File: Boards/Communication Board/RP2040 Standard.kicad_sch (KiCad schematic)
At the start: 38 parts, among them J1 BM03B-SRSS-TBLFSN, J4 DX07S016JA1R1500, U1 W25Q128JVSIQ TR, U5 ESD7L5.0DT5G, U6 ST1L05APU33R

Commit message: COMS
Acho que já está tudo de footprints que tinha que fazer na Communication Board
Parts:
- CV1, CV10, CV11, CV12, CV13, CV14, CV17, CV18, CV2, CV3, CV4, CV5, CV6, CV7, CV8, CV9: footprint Capacitor_SMD:C_0201_0603Metric -> CAP_GCM155_MUR:CAP_GCM155_MUR
- CV15, CV16: footprint Capacitor_SMD:C_0201_0603Metric -> GRM15x:GRM15x
- J1: footprint CONN_BM03B-SRSS-TBLFSN_JST -> SWD_Con:CONN_BM03B-SRSS-TBLFSN_JST
- J4: footprint DX07S016JA1R1500:JAE_DX07S016JA1R1500 -> USBC-DX07S016JA1:JAE_DX07S016JA1R1500
- R1, R4, R5, R6, R7, R8, R9, RC1: footprint Resistor_SMD:R_0201_0603Metric -> RC0402N_VIS:RC0402N_VIS
- R2, R3: footprint Resistor_SMD:R_0201_0603Metric -> KTR03EZPF27R0:RES_R0603_ROM
- S3, S4: footprint TL3305CF160QG:SW_TL3305CF160QG -> E-Switch_7mm:SW_TL3305CF160QG
- U1: footprint SOIC_208MIL_WIN -> NOR Flash:SOIC_208MIL_WIN
- U5: footprint SOT-723_0P85X1P25_ONS -> ESD7L5-Diode:SOT-723_0P85X1P25_ONS
- U6: footprint DFN_5APU33R_STM -> LDO ST1L05A:DFN_5APU33R_STM
- XTAL1: footprint ASE-3.2X2.5_ABR -> AS12MHz:ASE-3.2X2.5_ABR
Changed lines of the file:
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@@
 			)
 		)
-		(property "Footprint" "SOIC_208MIL_WIN"
+		(property "Footprint" "NOR Flash:SOIC_208MIL_WIN"
 			(at 180.975 45.72 0)
 			(effects
@@
 			)
 		)
-		(property "Footprint" "Capacitor_SMD:C_0201_0603Metric"
+		(property "Footprint" "CAP_GCM155_MUR:CAP_GCM155_MUR"
 			(at 132.08 177.4698 0)
 			(effects
@@
 			)
 		)
-		(property "Footprint" "DX07S016JA1R1500:JAE_DX07S016JA1R1500"
+		(property "Footprint" "USBC-DX07S016JA1:JAE_DX07S016JA1R1500"
 			(at 235.585 134.62 0)
 			(effects
@@
 			)
 		)
-		(property "Footprint" "Capacitor_SMD:C_0201_0603Metric"
+		(property "Footprint" "CAP_GCM155_MUR:CAP_GCM155_MUR"
 			(at 94.3102 50.165 0)
 			(effects
@@
 			)
 		)
-		(property "Footprint" "Capacitor_SMD:C_0201_0603Metric"
+		(property "Footprint" "CAP_GCM155_MUR:CAP_GCM155_MUR"
 			(at 32.6898 61.595 0)
 			(effects
@@
 			)
 		)
-		(property "Footprint" "ASE-3.2X2.5_ABR"
+		(property "Footprint" "AS12MHz:ASE-3.2X2.5_ABR"
 			(at 57.15 182.88 0)
 			(effects
@@
 			)
 		)
-		(property "Footprint" "Resistor_SMD:R_0201_0603Metric"
+		(property "Footprint" "KTR03EZPF27R0:RES_R0603_ROM"
 			(at 41.275 78.867 90)
 			(effects
@@
 			)
 		)
-		(property "Footprint" "Capacitor_SMD:C_0201_0603Metric"
+		(property "Footprint" "CAP_GCM155_MUR:CAP_GCM155_MUR"
 			(at 64.4398 42.545 0)
 			(effects
@@
 			)
 		)
-		(property "Footprint" "Capacitor_SMD:C_0201_0603Metric"
+		(property "Footprint" "CAP_GCM155_MUR:CAP_GCM155_MUR"
 			(at 101.2952 50.165 0)
 			(effects
@@
 			)
 		)
-		(property "Footprint" "SOT-723_0P85X1P25_ONS"
+		(property "Footprint" "ESD7L5-Diode:SOT-723_0P85X1P25_ONS"
 			(at 202.565 136.525 0)
 			(effects
@@
 			)
 		)
-		(property "Footprint" "Capacitor_SMD:C_0201_0603Metric"
+		(property "Footprint" "CAP_GCM155_MUR:CAP_GCM155_MUR"
 			(at 122.2502 50.165 0)
 			(effects
@@
 			)
 		)
-		(property "Footprint" "Capacitor_SMD:C_0201_0603Metric"
+		(property "Footprint" "CAP_GCM155_MUR:CAP_GCM155_MUR"
 			(at 129.2352 50.165 0)
 			(effects
@@
 			)
 		)
-		(property "Footprint" "Capacitor_SMD:C_0201_0603Metric"
+		(property "Footprint" "CAP_GCM155_MUR:CAP_GCM155_MUR"
 			(at 272.7452 41.91 0)
 			(effects
@@
 			)
 		)
-		(property "Footprint" "TL3305CF160QG:SW_TL3305CF160QG"
+		(property "Footprint" "E-Switch_7mm:SW_TL3305CF160QG"
 			(at 33.02 50.8 0)
 			(effects
@@
 			)
 		)
-		(property "Footprint" "Resistor_SMD:R_0201_0603Metric"
+		(property "Footprint" "RC0402N_VIS:RC0402N_VIS"
 			(at 55.372 177.8 90)
 			(effects
@@
 			)
 		)
-		(property "Footprint" "DFN_5APU33R_STM"
+		(property "Footprint" "LDO ST1L05A:DFN_5APU33R_STM"
 			(at 202.565 83.82 0)
 			(effects
@@
 			)
 		)
-		(property "Footprint" "Capacitor_SMD:C_0201_0603Metric"
+		(property "Footprint" "CAP_GCM155_MUR:CAP_GCM155_MUR"
 			(at 64.4652 62.23 0)
 			(effects
@@
 			)
 		)
-		(property "Footprint" "Resistor_SMD:R_0201_0603Metric"
+		(property "Footprint" "RC0402N_VIS:RC0402N_VIS"
 			(at 183.642 135.89 90)
 			(effects
@@
 			)
 		)
-		(property "Footprint" "Capacitor_SMD:C_0201_0603Metric"
+		(property "Footprint" "CAP_GCM155_MUR:CAP_GCM155_MUR"
 			(at 136.2202 50.165 0)
 			(effects
@@
 			)
 		)
-		(property "Footprint" "Capacitor_SMD:C_0201_0603Metric"
+		(property "Footprint" "CAP_GCM155_MUR:CAP_GCM155_MUR"
 			(at 87.3252 50.165 0)
 			(effects
@@
 			)
 		)
-		(property "Footprint" "Resistor_SMD:R_0201_0603Metric"
+		(property "Footprint" "KTR03EZPF27R0:RES_R0603_ROM"
 			(at 41.275 79.883 90)
 			(effects
@@
 			)
 		)
-		(property "Footprint" "Capacitor_SMD:C_0201_0603Metric"
+		(property "Footprint" "CAP_GCM155_MUR:CAP_GCM155_MUR"
 			(at 190.1698 89.535 0)
 			(effects
@@
 			)
 		)
-		(property "Footprint" "TL3305CF160QG:SW_TL3305CF160QG"
+		(property "Footprint" "E-Switch_7mm:SW_TL3305CF160QG"
 			(at 161.925 31.75 0)
 			(effects
@@
 			)
 		)
-		(property "Footprint" "CONN_BM03B-SRSS-TBLFSN_JST"
+		(property "Footprint" "SWD_Con:CONN_BM03B-SRSS-TBLFSN_JST"
 			(at 35.56 140.335 0)
 			(effects
@@
 			)
 		)
-		(property "Footprint" "Capacitor_SMD:C_0201_0603Metric"
+		(property "Footprint" "GRM15x:GRM15x"
 			(at 177.4698 90.17 0)
 			(effects
@@
 			)
 		)
-		(property "Footprint" "Resistor_SMD:R_0201_0603Metric"
+		(property "Footprint" "RC0402N_VIS:RC0402N_VIS"
 			(at 41.91 133.477 90)
 			(effects
@@
 			)
 		)
-		(property "Footprint" "Capacitor_SMD:C_0201_0603Metric"
+		(property "Footprint" "CAP_GCM155_MUR:CAP_GCM155_MUR"
 			(at 56.8198 42.545 0)
 			(effects
@@
 			)
 		)
-		(property "Footprint" "Resistor_SMD:R_0201_0603Metric"
+		(property "Footprint" "RC0402N_VIS:RC0402N_VIS"
 			(at 43.942 64.77 90)
 			(effects
@@
 			)
 		)
-		(property "Footprint" "Resistor_SMD:R_0201_0603Metric"
+		(property "Footprint" "RC0402N_VIS:RC0402N_VIS"
 			(at 177.927 40.005 90)
 			(effects
@@
 			)
 		)
-		(property "Footprint" "Capacitor_SMD:C_0201_0603Metric"
+		(property "Footprint" "CAP_GCM155_MUR:CAP_GCM155_MUR"
 			(at 115.2652 50.165 0)
 			(effects
@@
 			)
 		)
-		(property "Footprint" "Capacitor_SMD:C_0201_0603Metric"
+		(property "Footprint" "GRM15x:GRM15x"
 			(at 190.1698 85.725 0)
 			(effects
@@
 			)
 		)
-		(property "Footprint" "Resistor_SMD:R_0201_0603Metric"
+		(property "Footprint" "RC0402N_VIS:RC0402N_VIS"
 			(at 189.357 137.795 90)
 			(effects
@@
 			)
 		)
-		(property "Footprint" "Capacitor_SMD:C_0201_0603Metric"
+		(property "Footprint" "CAP_GCM155_MUR:CAP_GCM155_MUR"
 			(at 108.2802 50.165 0)
 			(effects
@@
 			)
 		)
-		(property "Footprint" "Resistor_SMD:R_0201_0603Metric"
+		(property "Footprint" "RC0402N_VIS:RC0402N_VIS"
 			(at 18.542 65.405 90)
 			(effects
@@
 			)
 		)
-		(property "Footprint" "Capacitor_SMD:C_0201_0603Metric"
+		(property "Footprint" "CAP_GCM155_MUR:CAP_GCM155_MUR"
 			(at 87.3252 59.69 0)
 			(effects
@@
 			)
 		)
-		(property "Footprint" "Resistor_SMD:R_0201_0603Metric"
+		(property "Footprint" "RC0402N_VIS:RC0402N_VIS"
 			(at 41.91 138.557 90)
 			(effects

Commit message: Mudança de nome das footprints
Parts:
- CV1, CV10, CV11, CV12, CV13, CV14, CV17, CV18, CV2, CV3, CV4, CV5, CV6, CV7, CV8, CV9: footprint CAP_GCM155_MUR:CAP_GCM155_MUR -> Capacitor_0402:Capacitor_0402
- CV15, CV16: footprint GRM15x:GRM15x -> C_4uF7_0402:C_4uF7_0402
- R1, R4, R5, R6, R7, R8: footprint RC0402N_VIS:RC0402N_VIS -> RES_0402:RES_0402
- R2, R3: footprint KTR03EZPF27R0:RES_R0603_ROM -> RES_R0603_27:RES_R0603_27
- R9, RC1: footprint RC0402N_VIS:RC0402N_VIS -> R_0805_5K1:R_0805_5K1
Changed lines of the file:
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@@
 			)
 		)
-		(property "Footprint" "CAP_GCM155_MUR:CAP_GCM155_MUR"
+		(property "Footprint" "Capacitor_0402:Capacitor_0402"
 			(at 132.08 177.4698 0)
 			(effects
@@
 			)
 		)
-		(property "Footprint" "CAP_GCM155_MUR:CAP_GCM155_MUR"
+		(property "Footprint" "Capacitor_0402:Capacitor_0402"
 			(at 94.3102 50.165 0)
 			(effects
@@
 			)
 		)
-		(property "Footprint" "CAP_GCM155_MUR:CAP_GCM155_MUR"
+		(property "Footprint" "Capacitor_0402:Capacitor_0402"
 			(at 32.6898 61.595 0)
 			(effects
@@
 			)
 		)
-		(property "Footprint" "KTR03EZPF27R0:RES_R0603_ROM"
+		(property "Footprint" "RES_R0603_27:RES_R0603_27"
 			(at 41.275 78.867 90)
 			(effects
@@
 			)
 		)
-		(property "Footprint" "CAP_GCM155_MUR:CAP_GCM155_MUR"
+		(property "Footprint" "Capacitor_0402:Capacitor_0402"
 			(at 64.4398 42.545 0)
 			(effects
@@
 			)
 		)
-		(property "Footprint" "CAP_GCM155_MUR:CAP_GCM155_MUR"
+		(property "Footprint" "Capacitor_0402:Capacitor_0402"
 			(at 101.2952 50.165 0)
 			(effects
@@
 			)
 		)
-		(property "Footprint" "CAP_GCM155_MUR:CAP_GCM155_MUR"
+		(property "Footprint" "Capacitor_0402:Capacitor_0402"
 			(at 122.2502 50.165 0)
 			(effects
@@
 			)
 		)
-		(property "Footprint" "CAP_GCM155_MUR:CAP_GCM155_MUR"
+		(property "Footprint" "Capacitor_0402:Capacitor_0402"
 			(at 129.2352 50.165 0)
 			(effects
@@
 			)
 		)
-		(property "Footprint" "CAP_GCM155_MUR:CAP_GCM155_MUR"
+		(property "Footprint" "Capacitor_0402:Capacitor_0402"
 			(at 272.7452 41.91 0)
 			(effects
@@
 			)
 		)
-		(property "Footprint" "RC0402N_VIS:RC0402N_VIS"
+		(property "Footprint" "RES_0402:RES_0402"
 			(at 55.372 177.8 90)
 			(effects
@@
 			)
 		)
-		(property "Footprint" "CAP_GCM155_MUR:CAP_GCM155_MUR"
+		(property "Footprint" "Capacitor_0402:Capacitor_0402"
 			(at 64.4652 62.23 0)
 			(effects
@@
 			)
 		)
-		(property "Footprint" "RC0402N_VIS:RC0402N_VIS"
+		(property "Footprint" "R_0805_5K1:R_0805_5K1"
 			(at 183.642 135.89 90)
 			(effects
@@
 			)
 		)
-		(property "Footprint" "CAP_GCM155_MUR:CAP_GCM155_MUR"
+		(property "Footprint" "Capacitor_0402:Capacitor_0402"
 			(at 136.2202 50.165 0)
 			(effects
@@
 			)
 		)
-		(property "Footprint" "CAP_GCM155_MUR:CAP_GCM155_MUR"
+		(property "Footprint" "Capacitor_0402:Capacitor_0402"
 			(at 87.3252 50.165 0)
 			(effects
@@
 			)
 		)
-		(property "Footprint" "KTR03EZPF27R0:RES_R0603_ROM"
+		(property "Footprint" "RES_R0603_27:RES_R0603_27"
 			(at 41.275 79.883 90)
 			(effects
@@
 			)
 		)
-		(property "Footprint" "CAP_GCM155_MUR:CAP_GCM155_MUR"
+		(property "Footprint" "Capacitor_0402:Capacitor_0402"
 			(at 190.1698 89.535 0)
 			(effects
@@
 			)
 		)
-		(property "Footprint" "GRM15x:GRM15x"
+		(property "Footprint" "C_4uF7_0402:C_4uF7_0402"
 			(at 177.4698 90.17 0)
 			(effects
@@
 			)
 		)
-		(property "Footprint" "RC0402N_VIS:RC0402N_VIS"
+		(property "Footprint" "RES_0402:RES_0402"
 			(at 41.91 133.477 90)
 			(effects
@@
 			)
 		)
-		(property "Footprint" "CAP_GCM155_MUR:CAP_GCM155_MUR"
+		(property "Footprint" "Capacitor_0402:Capacitor_0402"
 			(at 56.8198 42.545 0)
 			(effects
@@
 			)
 		)
-		(property "Footprint" "RC0402N_VIS:RC0402N_VIS"
+		(property "Footprint" "RES_0402:RES_0402"
 			(at 43.942 64.77 90)
 			(effects
@@
 			)
 		)
-		(property "Footprint" "RC0402N_VIS:RC0402N_VIS"
+		(property "Footprint" "RES_0402:RES_0402"
 			(at 177.927 40.005 90)
 			(effects
@@
 			)
 		)
-		(property "Footprint" "CAP_GCM155_MUR:CAP_GCM155_MUR"
+		(property "Footprint" "Capacitor_0402:Capacitor_0402"
 			(at 115.2652 50.165 0)
 			(effects
@@
 			)
 		)
-		(property "Footprint" "GRM15x:GRM15x"
+		(property "Footprint" "C_4uF7_0402:C_4uF7_0402"
 			(at 190.1698 85.725 0)
 			(effects
@@
 			)
 		)
-		(property "Footprint" "RC0402N_VIS:RC0402N_VIS"
+		(property "Footprint" "R_0805_5K1:R_0805_5K1"
 			(at 189.357 137.795 90)
 			(effects
@@
 			)
 		)
-		(property "Footprint" "CAP_GCM155_MUR:CAP_GCM155_MUR"
+		(property "Footprint" "Capacitor_0402:Capacitor_0402"
 			(at 108.2802 50.165 0)
 			(effects
@@
 			)
 		)
-		(property "Footprint" "RC0402N_VIS:RC0402N_VIS"
+		(property "Footprint" "RES_0402:RES_0402"
 			(at 18.542 65.405 90)
 			(effects
@@
 			)
 		)
-		(property "Footprint" "CAP_GCM155_MUR:CAP_GCM155_MUR"
+		(property "Footprint" "Capacitor_0402:Capacitor_0402"
 			(at 87.3252 59.69 0)
 			(effects
@@
 			)
 		)
-		(property "Footprint" "RC0402N_VIS:RC0402N_VIS"
+		(property "Footprint" "RES_0402:RES_0402"
 			(at 41.91 138.557 90)
 			(effects

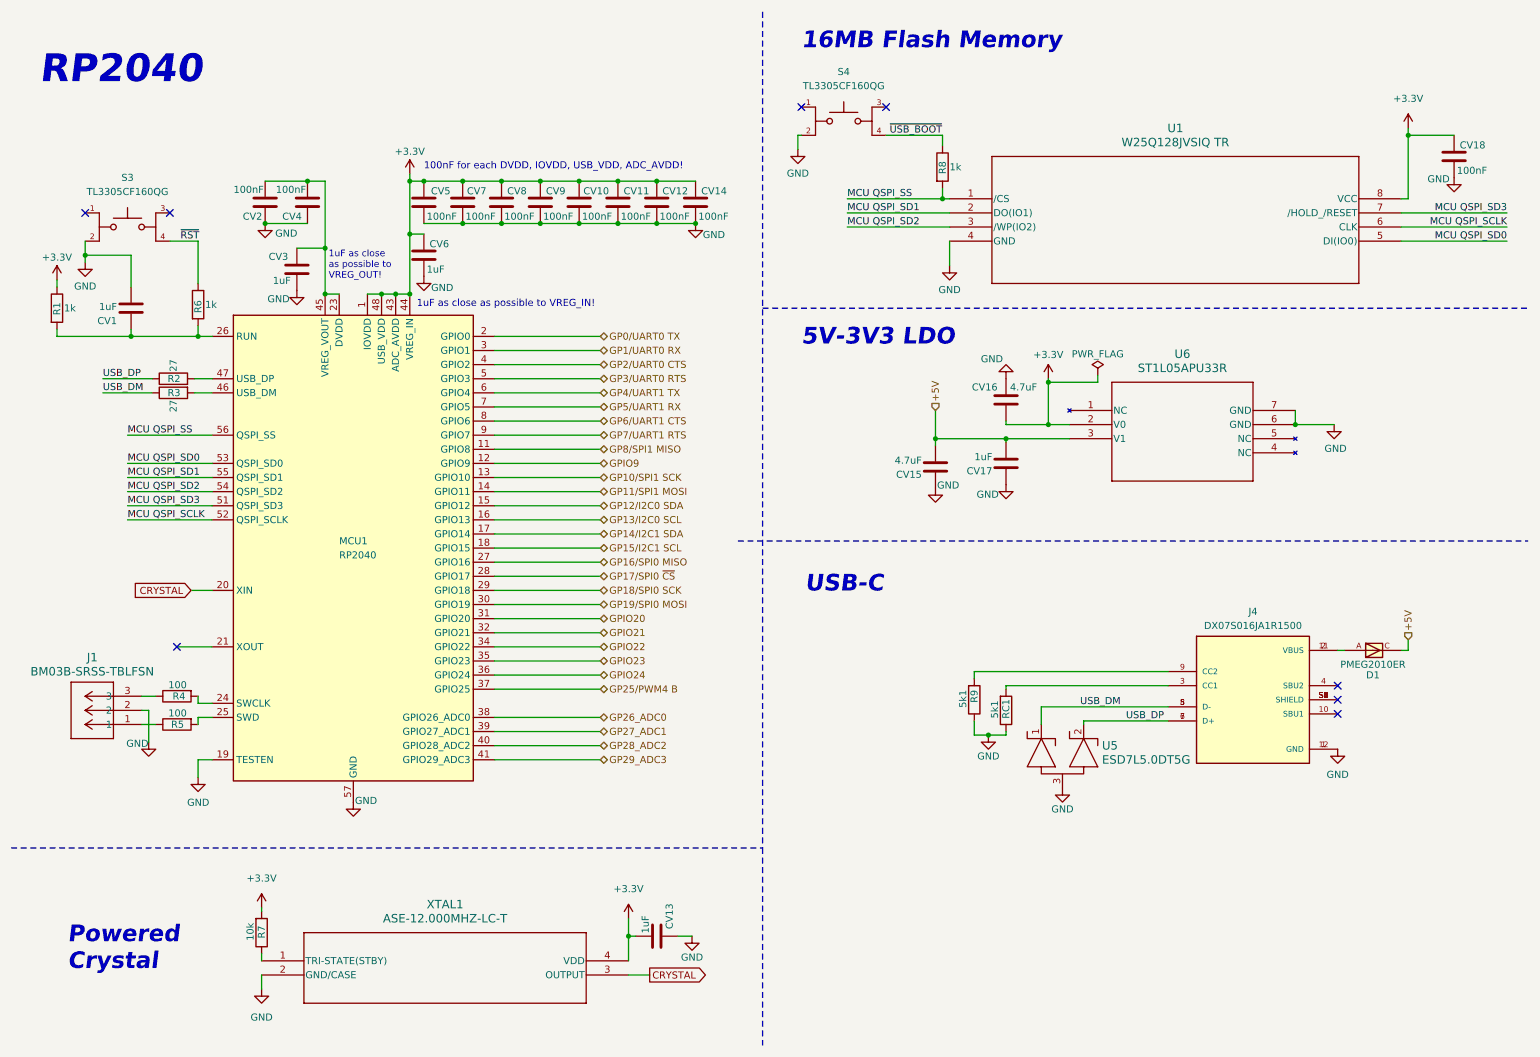
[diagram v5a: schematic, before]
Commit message: changes in RP2040 design
GPIO25 LED is now part of RP2040 Standard
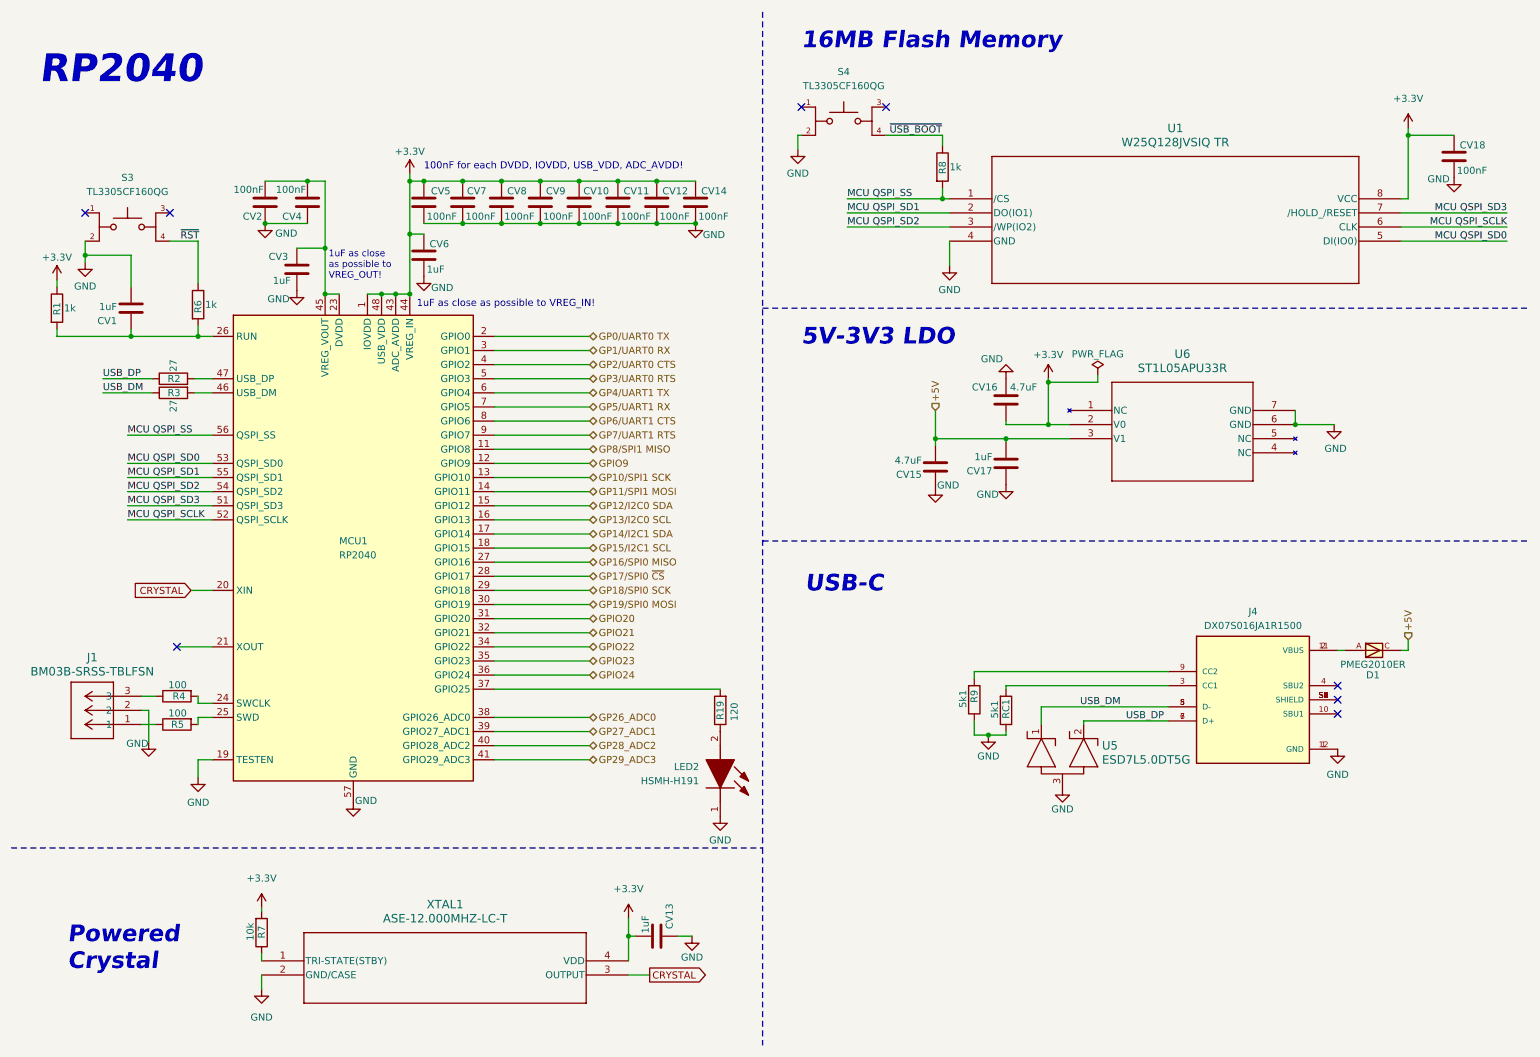
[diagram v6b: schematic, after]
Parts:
- added LED2: HSMH-H191, Red SMD LED:HSMHH191, symbol Red SMD LED:HSMH-H191
- added R19: 120, RES_0402:RES_0402, symbol Device:R
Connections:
- net GND: now also LED2.1 (K)
- net GP25/PWM4 B: no longer names the net of MCU1.37 (GPIO25)
- net GP25/PWM4 B: now also R19.2
- new net: LED2.2 (A), R19.1
